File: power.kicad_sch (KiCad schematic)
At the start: 101 parts, among them U41 TPS7A8801RTJR, U42 TPS7A8801RTJR, U43 TPS61252DSG, U44 TPSM863252RDXR, U45 TPS7A3301RGW, U46 TPSM863252RDXR

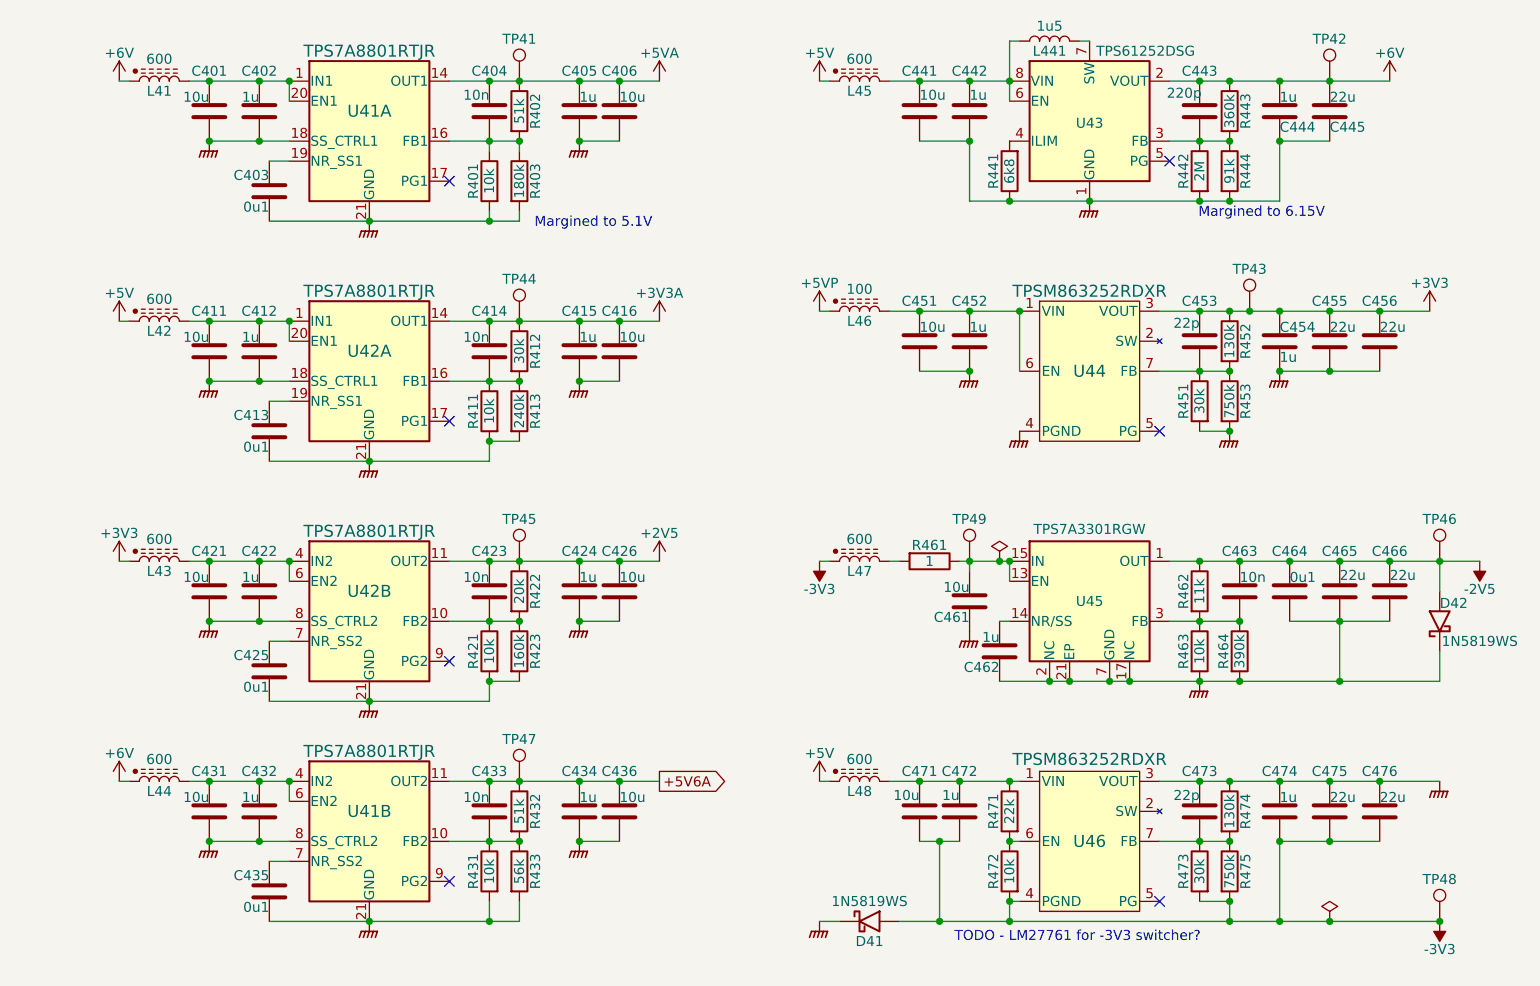
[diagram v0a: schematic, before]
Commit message: Whew.  DACs routed
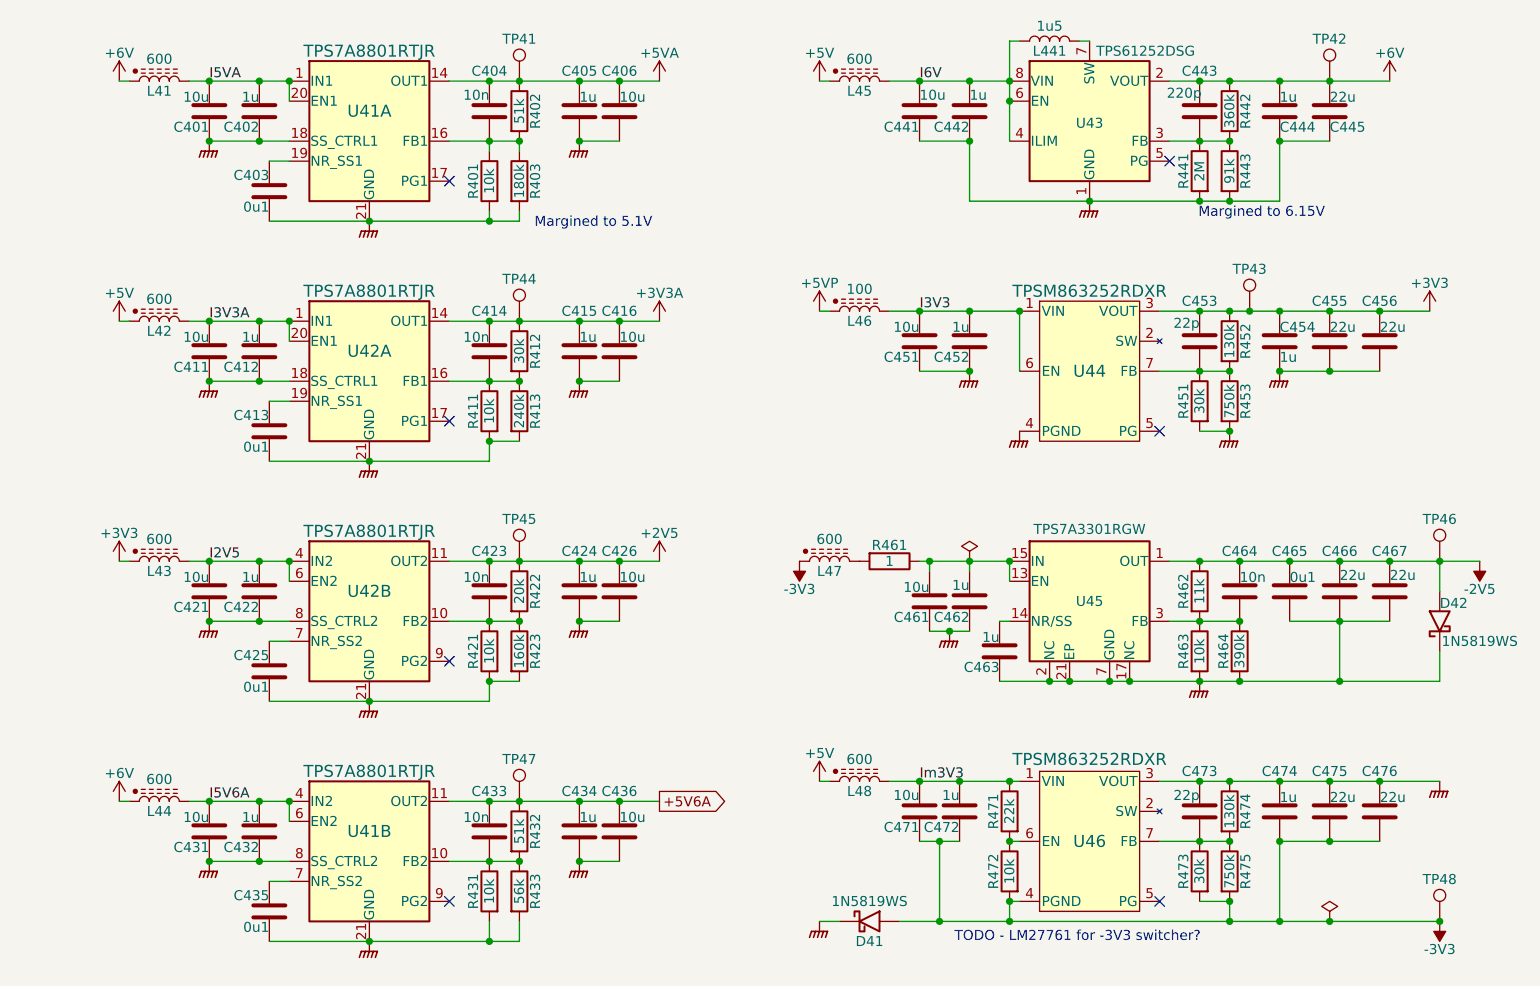
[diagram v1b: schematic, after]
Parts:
- removed R441: 6k8, Resistor_SMD:R_0603_1608Metric, symbol Device:R
- removed TP49: TestPoint, Parts:TestPoint, symbol Connector:TestPoint
- added C462: 1u, Capacitor_SMD:C_0402_1005Metric, symbol Device:C
- renumbered C462 to C463, C463 to C464, C464 to C465, C465 to C466, C466 to C467, R442 to R441, R443 to R442, R444 to R443
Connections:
- net GNDPWR: now also C462.2
- net Im3V3: now reaches C471.1, C472.1, L48.2, R471.1, U46.1 (VIN)
- net I2V5: now reaches C421.1, C422.1, L43.2, U42.4 (IN2), U42.5 (IN2), U42.6 (EN2)
- net I6V: now reaches U43.4 (ILIM)
- net I6V: now also C441.1, C442.1, L441.1, L45.2, U43.6 (EN), U43.8 (VIN)
- net I5V6A: now reaches C431.1, C432.1, L44.2, U41.4 (IN2), U41.5 (IN2), U41.6 (EN2)
- net I5VA: now reaches C401.1, C402.1, L41.2, U41.1 (IN1), U41.2 (IN1), U41.20 (EN1)
- net at C461.1, R461.1, U45.13 (EN)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: now also C462.1
- net I3V3A: now reaches C411.1, C412.1, L42.2, U42.1 (IN1), U42.2 (IN1), U42.20 (EN1)
- net I3V3: now reaches C451.1, C452.1, L46.2, U44.1 (VIN), U44.6 (EN)
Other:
- moved on the sheet: C431, C432, C433, C434, C435, C436, C461, L44, L47, R431, R432, R433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

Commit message: Tweaks following spice simulation.
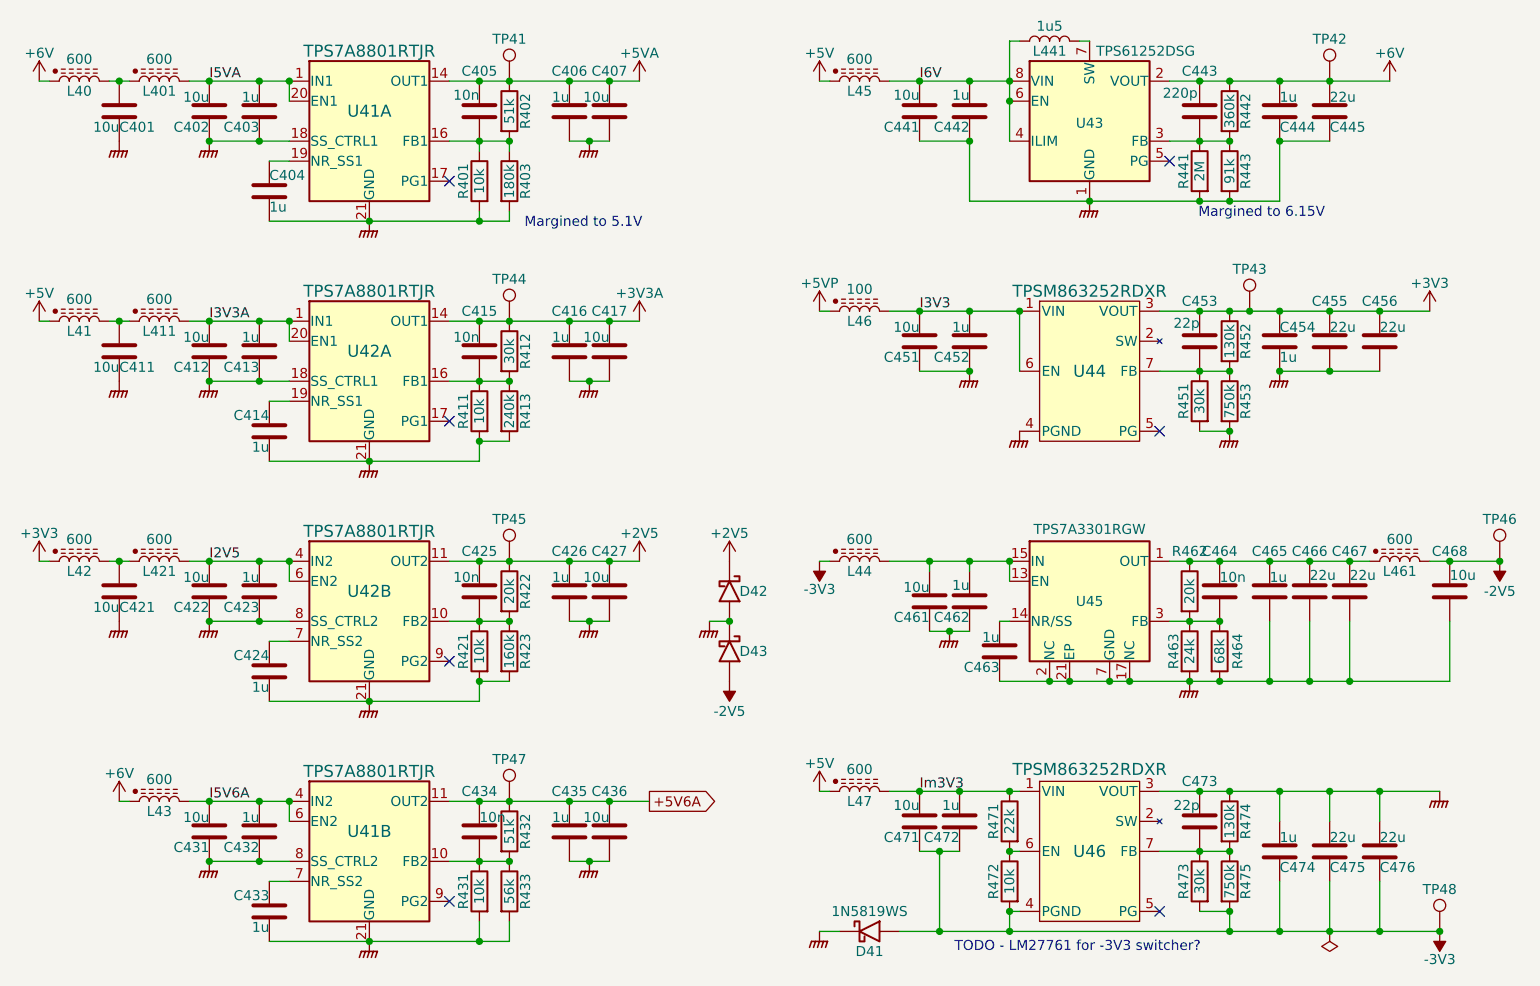
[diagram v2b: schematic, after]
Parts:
- removed R461: 1, Resistor_SMD:R_0603_1608Metric, symbol Device:R
- added C401, C411, C421, C468: 10u, Capacitor_SMD:C_0603_1608Metric, symbol Device:C
- added D42: 1N5819WS, Diode_SMD:D_SOD-323, symbol Parts:1N5819WS
- added L401, L411, L421, L461: 600, Inductor_SMD:L_0603_1608Metric, symbol Parts:L_Ferrite_Power
- C404: renamed from C403; value 0u1 -> 1u; LCSC C307331 -> C52923
- C414: renamed from C413; value 0u1 -> 1u; LCSC C307331 -> C52923
- C424: renamed from C425; value 0u1 -> 1u; LCSC C307331 -> C52923
- C433: renamed from C435; value 0u1 -> 1u; LCSC C307331 -> C52923
- C443: footprint Capacitor_SMD:C_0603_1608Metric -> Capacitor_SMD:C_0402_1005Metric; LCSC C1664 -> C1530
- C465: value 0u1 -> 1u; LCSC C307331 -> C52923
- R462: value 11k -> 20k; footprint Resistor_SMD:R_0603_1608Metric -> Resistor_SMD:R_0402_1005Metric; LCSC C25950 -> C25765
- R463: value 10k -> 24k; footprint Resistor_SMD:R_0402_1005Metric -> Resistor_SMD:R_0603_1608Metric; LCSC C25744 -> C23352
- R464: value 390k -> 68k; LCSC C23150 -> C23231
- renumbered C401 to C402, C402 to C403, C404 to C405, C405 to C406, C406 to C407, C411 to C412, C412 to C413, C414 to C415, C415 to C416, C416 to C417, C421 to C422, C422 to C423, C423 to C425, C424 to C426, C426 to C427, C433 to C434, C434 to C435, D42 to D43, L41 to L40, L42 to L41, L43 to L42, L44 to L43, L47 to L44, L48 to L47
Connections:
- net +2V5: now also D42.1 (K)
- net -2V5: now also C468.1, L461.2; no longer C464.2, C465.2, C466.1, C467.1, R462.1, U45.1 (OUT), U45.20 (OUT)
- net GNDPWR: now also C401.2, C411.2, C421.2, C468.2, D42.2 (A)
- net I2V5: now also L421.2; no longer L42.2
- net I3V3A: now also L411.2; no longer L41.2
- net I5VA: now also L401.2; no longer L40.2
- net at R462.2, R463.1, R464.1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: now also C464.2; no longer C464.1
- net at L44.2: now also C461.1, C462.1, U45.13 (EN), U45.15 (IN), U45.16 (IN)
- new net: C411.1, L41.2, L411.1
- new net: C464.1, C465.2, C466.1, C467.1, L461.1, R462.1, U45.1 (OUT), U45.20 (OUT)
- new net: C421.1, L42.2, L421.1
- new net: C401.1, L40.2, L401.1
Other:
- moved on the sheet: C405, C406, C407, C415, C416, C417, C425, C426, C427, C434, C435, C436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

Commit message: About to delete scan...
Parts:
- TP41, TP42, TP43, TP44, TP45, TP46, TP47, TP48: Stock (none) -> -
- U41, U42: Stock (none) -> 6
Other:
- moved on the sheet: C464, C474, C475, C476, R462

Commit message: Most blocks there....
About to restore scan.
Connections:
- net -2V5: now also C464.1, C465.2, C466.1, C467.1, R462.1, U45.1 (OUT), U45.20 (OUT); no longer C468.1, L461.2
- net Im2V5: now reaches C461.1, C462.1, U45.13 (EN), U45.15 (IN), U45.16 (IN)
- net Im2V5: now also L461.2; no longer L44.2
- new net: C468.1, L44.2, L461.1
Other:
- moved on the sheet: C466, C467, C468, D42, D43, L44, L461, TP46, TP48

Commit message: Adjust voltage rails.
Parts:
- D41, D42, D43: footprint Diode_SMD:D_SOD-323 -> Parts:SOD-323
- TP41: value TestPoint -> 5V1
- TP42: value TestPoint -> 6V
- TP43, TP44: value TestPoint -> 3V3
- TP45: value TestPoint -> 2V5
- TP46: value TestPoint -> -2V5
- TP47: value TestPoint -> 5V6
- TP48: value TestPoint -> -3V3
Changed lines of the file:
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@@
 			)
 		)
-		(property "Value" "TestPoint"
+		(property "Value" "2V5"
 			(at 102.87 97.79 0)
 			(effects
@@
 			)
 		)
-		(property "Value" "TestPoint"
+		(property "Value" "5V1"
 			(at 102.87 36.83 0)
 			(effects
@@
 			)
 		)
-		(property "Value" "TestPoint"
+		(property "Value" "3V3"
 			(at 102.87 67.31 0)
 			(effects
@@
 			)
 		)
-		(property "Value" "TestPoint"
+		(property "Value" "-3V3"
 			(at 219.71 144.78 0)
 			(effects
@@
 			)
 		)
-		(property "Footprint" "Diode_SMD:D_SOD-323"
+		(property "Footprint" "Parts:SOD-323"
 			(at 126.365 86.36 0)
 			(effects
@@
 			)
 		)
-		(property "Value" "TestPoint"
+		(property "Value" "-2V5"
 			(at 219.71 97.79 0)
 			(effects
@@
 			)
 		)
-		(property "Value" "TestPoint"
+		(property "Value" "5V6"
 			(at 102.87 128.27 0)
 			(effects
@@
 			)
 		)
-		(property "Footprint" "Diode_SMD:D_SOD-323"
+		(property "Footprint" "Parts:SOD-323"
 			(at 126.365 78.74 0)
 			(effects
@@
 			)
 		)
-		(property "Value" "TestPoint"
+		(property "Value" "6V"
 			(at 207.01 36.83 0)
 			(effects
@@
 			)
 		)
-		(property "Footprint" "Diode_SMD:D_SOD-323"
+		(property "Footprint" "Parts:SOD-323"
 			(at 148.59 154.305 0)
 			(effects
@@
 			)
 		)
-		(property "Value" "TestPoint"
+		(property "Value" "3V3"
 			(at 196.85 66.04 0)
 			(effects

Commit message: Progress checkin.  About to redo FDA feedback again.
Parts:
- renumbered C453 to C41, C456 to C42
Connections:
- net -2V5: now also C465.1; no longer C465.2
- net GNDPWR: now also C463.2, C465.2; no longer C463.1, C465.1
- net at U45.14 (NR/SS): now also C463.1; no longer C463.2
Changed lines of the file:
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@@
 		(lib_id "Device:C")
 		(at 110.49 137.16 0)
-		(mirror y)
 		(unit 1)
 		(exclude_from_sim no)
@@
 		)
 		(property "Footprint" "Capacitor_SMD:C_0402_1005Metric"
-			(at 109.5248 140.97 0)
+			(at 111.4552 140.97 0)
 			(effects
 				(font
@@
 		(lib_id "Device:R")
 		(at 99.06 83.82 0)
-		(mirror y)
 		(unit 1)
 		(exclude_from_sim no)
@@
 		)
 		(property "Footprint" "Resistor_SMD:R_0402_1005Metric"
-			(at 100.838 83.82 90)
+			(at 97.282 83.82 90)
 			(effects
 				(font
@@
 		(lib_id "Device:C")
 		(at 115.57 137.16 0)
-		(mirror y)
 		(unit 1)
 		(exclude_from_sim no)
@@
 		)
 		(property "Footprint" "Capacitor_SMD:C_0603_1608Metric"
-			(at 114.6048 140.97 0)
+			(at 116.5352 140.97 0)
 			(effects
 				(font
@@
 		(lib_id "Device:R")
 		(at 190.5 53.34 0)
-		(mirror y)
 		(unit 1)
 		(exclude_from_sim no)
@@
 		)
 		(property "Footprint" "Resistor_SMD:R_0603_1608Metric"
-			(at 192.278 53.34 90)
+			(at 188.722 53.34 90)
 			(effects
 				(font
@@
 		(lib_id "Device:R")
 		(at 99.06 144.78 0)
-		(mirror y)
 		(unit 1)
 		(exclude_from_sim no)
@@
 		)
 		(property "Footprint" "Resistor_SMD:R_0402_1005Metric"
-			(at 100.838 144.78 90)
+			(at 97.282 144.78 90)
 			(effects
 				(font
@@
 		(lib_id "Device:R")
 		(at 190.5 143.51 0)
-		(mirror y)
 		(unit 1)
 		(exclude_from_sim no)
@@
 		)
 		(property "Footprint" "Resistor_SMD:R_0603_1608Metric"
-			(at 192.278 143.51 90)
+			(at 188.722 143.51 90)
 			(effects
 				(font
@@
 		(lib_id "Device:C")
 		(at 199.39 106.68 0)
-		(mirror x)
 		(unit 1)
 		(exclude_from_sim no)
@@
 		)
 		(property "Footprint" "Capacitor_SMD:C_0402_1005Metric"
-			(at 200.3552 102.87 0)
+			(at 200.3552 110.49 0)
 			(effects
 				(font
@@
 		(lib_id "Device:C")
 		(at 99.06 137.16 0)
-		(mirror y)
 		(unit 1)
 		(exclude_from_sim no)
@@
 		)
 		(property "Footprint" "Capacitor_SMD:C_0603_1608Metric"
-			(at 98.0948 140.97 0)
+			(at 100.0252 140.97 0)
 			(effects
 				(font
@@
 		(lib_id "Device:R")
 		(at 99.06 114.3 0)
-		(mirror y)
 		(unit 1)
 		(exclude_from_sim no)
@@
 		)
 		(property "Footprint" "Resistor_SMD:R_0402_1005Metric"
-			(at 100.838 114.3 90)
+			(at 97.282 114.3 90)
 			(effects
 				(font
@@
 		(on_board yes)
 		(dnp no)
-		(property "Reference" "C453"
+		(property "Reference" "C41"
 			(at 190.5 69.85 0)
 			(effects
@@
 			(project "lincal"
 				(path "/b054cef4-39e3-49d8-aff0-7ba5a206c187/98a8b958-69ae-452b-9f02-aef214a697d8"
-					(reference "C453")
+					(reference "C41")
 					(unit 1)
 				)
@@
 		(lib_id "Device:C")
 		(at 165.1 114.3 0)
-		(mirror x)
 		(unit 1)
 		(exclude_from_sim no)
@@
 		)
 		(property "Value" "1u"
-			(at 165.1 112.522 0)
+			(at 165.1 112.268 0)
 			(effects
 				(font
@@
 		)
 		(property "Footprint" "Capacitor_SMD:C_0402_1005Metric"
-			(at 166.0652 110.49 0)
+			(at 166.0652 118.11 0)
 			(effects
 				(font
@@
 		(on_board yes)
 		(dnp no)
-		(property "Reference" "C456"
+		(property "Reference" "C42"
 			(at 213.36 69.85 0)
 			(effects
@@
 			(project "lincal"
 				(path "/b054cef4-39e3-49d8-aff0-7ba5a206c187/98a8b958-69ae-452b-9f02-aef214a697d8"
-					(reference "C456")
+					(reference "C42")
 					(unit 1)
 				)
@@
 		(lib_id "Device:R")
 		(at 99.06 54.61 0)
-		(mirror y)
 		(unit 1)
 		(exclude_from_sim no)
@@
 		)
 		(property "Footprint" "Resistor_SMD:R_0402_1005Metric"
-			(at 100.838 54.61 90)
+			(at 97.282 54.61 90)
 			(effects
 				(font
@@
 		(lib_id "Device:R")
 		(at 190.5 82.55 0)
-		(mirror y)
 		(unit 1)
 		(exclude_from_sim no)
@@
 		)
 		(property "Footprint" "Resistor_SMD:R_0603_1608Metric"
-			(at 192.278 82.55 90)
+			(at 188.722 82.55 90)
 			(effects
 				(font

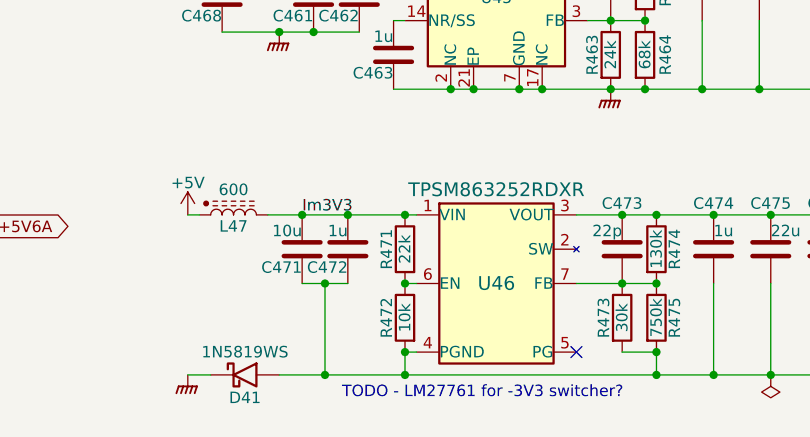
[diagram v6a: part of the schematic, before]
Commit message: Start to place within physical board size.
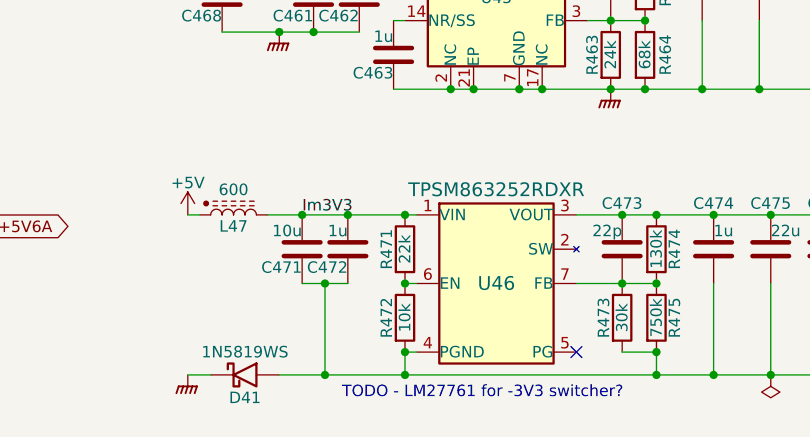
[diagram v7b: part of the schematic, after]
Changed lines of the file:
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@@
 		(lib_id "Device:R")
 		(at 166.37 143.51 0)
-		(mirror y)
 		(unit 1)
 		(exclude_from_sim no)
@@
 		)
 		(property "Footprint" "Resistor_SMD:R_0402_1005Metric"
-			(at 168.148 143.51 90)
+			(at 164.592 143.51 90)
 			(effects
 				(font
@@
 		(lib_id "Device:R")
 		(at 166.37 135.89 0)
-		(mirror y)
 		(unit 1)
 		(exclude_from_sim no)
@@
 		)
 		(property "Footprint" "Resistor_SMD:R_0402_1005Metric"
-			(at 168.148 135.89 90)
+			(at 164.592 135.89 90)
 			(effects
 				(font

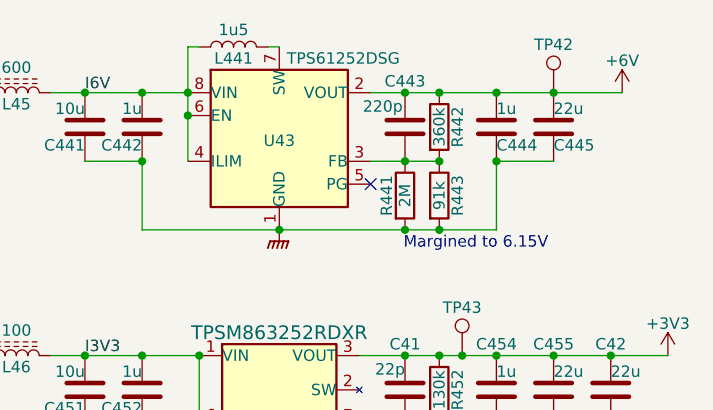
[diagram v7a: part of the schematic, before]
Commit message: Power mostly routed
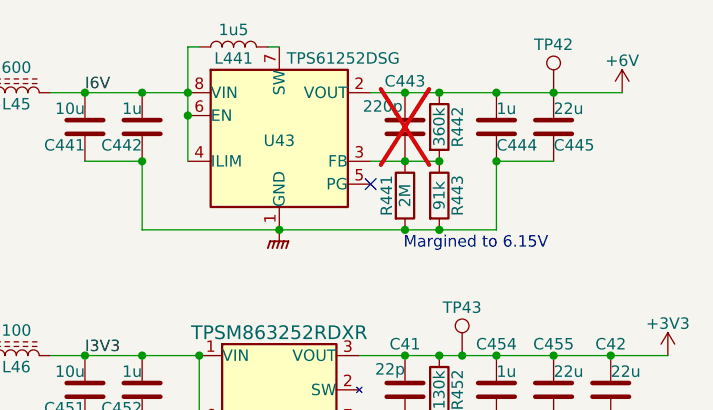
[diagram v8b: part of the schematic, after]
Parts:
- C443: footprint Capacitor_SMD:C_0402_1005Metric -> Capacitor_SMD:C_0603_1608Metric; LCSC C1530 -> (none); now not fitted
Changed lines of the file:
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@@
 		(in_bom yes)
 		(on_board yes)
-		(dnp no)
+		(dnp yes)
 		(property "Reference" "C443"
 			(at 190.5 40.64 0)
@@
 			)
 		)
-		(property "Footprint" "Capacitor_SMD:C_0402_1005Metric"
+		(property "Footprint" "Capacitor_SMD:C_0603_1608Metric"
 			(at 191.4652 49.53 0)
 			(effects
@@
 			)
 		)
-		(property "LCSC" "C1530"
+		(property "LCSC" ""
 			(at 190.5 45.72 0)
 			(effects
